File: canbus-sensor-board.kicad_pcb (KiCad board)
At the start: 4 copper layers, 34.5 x 15 mm, 43 parts, among them J1 Conn_ARM_SWD_TagConnect_TC203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, J10 Conn_01x04_Socket, J11 Conn_01x04_Socket, J2 CAN Term, J3 Conn_01x01, J4 Conn_01x01, J5 Conn_01x01, J6 Conn_01x01, J7 Conn_01x01, J8 Conn_01x02_Socket, J9 Conn_01x02_Socket, Q1 AO3400A, Q2 AO3400A, Q3 AO3400A, Q4 AO3400A, U1 L78L05_SOT89, U2 XC6206PxxxMR, U3 STM32F103C8Tx, U4 MCP2551-I-SN

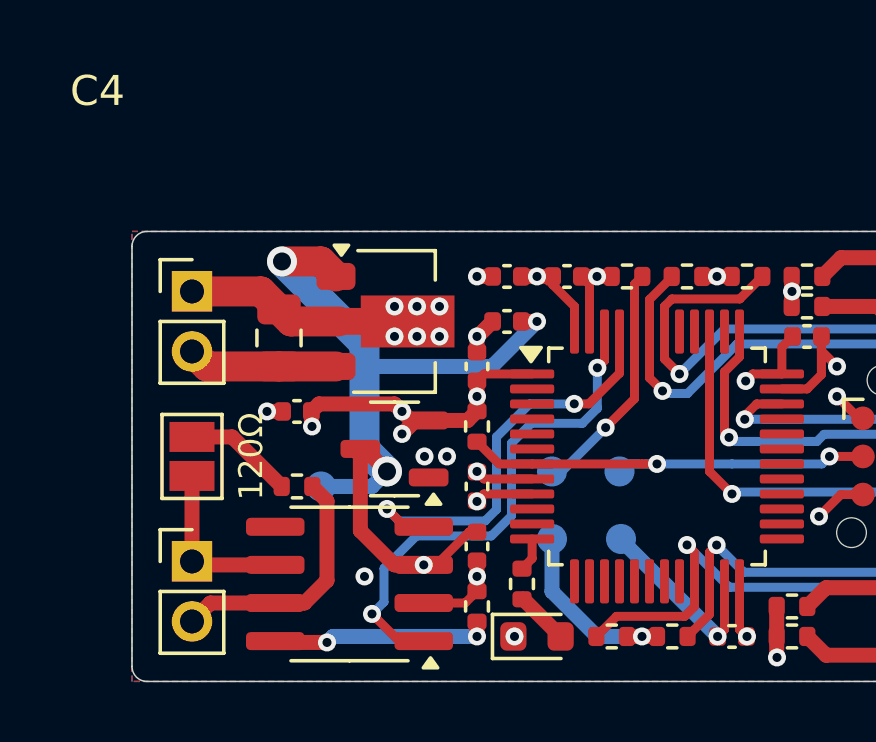
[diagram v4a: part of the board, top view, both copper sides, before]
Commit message: Also make 5V cap larger to have more error margin
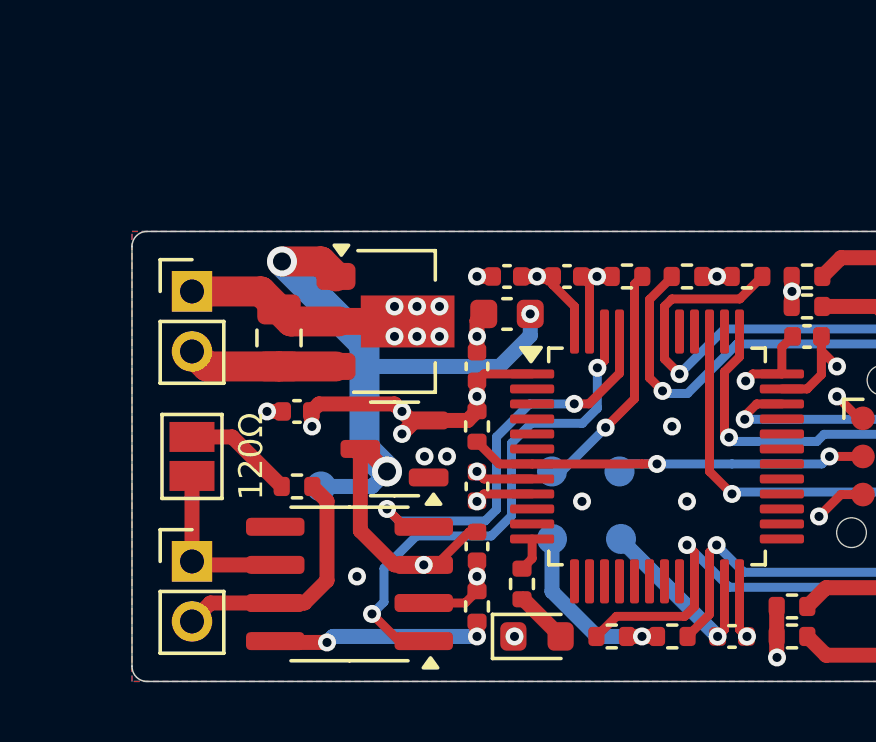
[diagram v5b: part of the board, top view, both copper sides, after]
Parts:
- C2: value 10u -> 10u >5V; footprint Capacitor_SMD:C_0402_1005Metric -> Capacitor_SMD:C_0603_1608Metric
- moved C2 0.25 mm to (35.0, 35.2)
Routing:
- net GND: track 27.8 -> 27.9 mm, vias 21 -> 24
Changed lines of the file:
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@@
 		(tags "SOT-89-3")
 		(property "Reference" "U1"
-			(at 0 -3.5 0)
+			(at -9.9 -7.68 0)
 			(layer "User.1")
 			(hide yes)
@@
 			)
 		)
-		(property "Reference" "C4"
-			(at -9.9 -7.68 0)
-			(layer "F.SilkS")
+		(property "Datasheet" "http://www.st.com/content/ccc/resource/technical/document/datasheet/15/55/e5/aa/23/5b/43/fd/CD00000446.pdf/files/CD00000446.pdf/jcr:content/translations/en.CD00000446.pdf"
+			(at 0 0 0)
+			(unlocked yes)
+			(layer "F.Fab")
+			(hide yes)
 			(effects
 				(font
@@
 			)
 		)
-		(property "Datasheet" "http://www.st.com/content/ccc/resource/technical/document/datasheet/15/55/e5/aa/23/5b/43/fd/CD00000446.pdf/files/CD00000446.pdf/jcr:content/translations/en.CD00000446.pdf"
-			(at 0 0 0)
-			(unlocked yes)
-			(layer "F.Fab")
-			(hide yes)
-			(effects
-				(font
-					(size 1 1)
-					(thickness 0.15)
-				)
-			)
-		)
 		(property ki_fp_filters "SOT?89*")
 		(sheetname "Root")
@@
 		(tags "capacitor")
 		(property "Reference" "C1"
-			(at 0 -1.68 270)
+			(at 0 -1.68 -90)
 			(layer "User.1")
 			(hide yes)
@@
 		)
 		(property "Value" "10u >24V"
-			(at 0 1.68 270)
+			(at 0 1.68 -90)
 			(layer "F.Fab")
 			(effects
@@
 		)
 		(fp_text user "${REFERENCE}"
-			(at 0 0 270)
+			(at 0 0 -90)
 			(layer "F.Fab")
 			(effects
@@
 		)
 	)
-	(footprint "Capacitor_SMD:C_0402_1005Metric"
+	(footprint "Capacitor_SMD:C_0603_1608Metric"
 		(layer "F.Cu")
-		(at 35 35.5 180)
-		(descr "Capacitor SMD 0402 (1005 Metric), square (rectangular) end terminal, IPC_7351 nominal, (Body size source: IPC-SM-782 page 76, https://www.pcb-3d.com/wordpress/wp-content/uploads/ipc-sm-782a_amendment_1_and_2.pdf), generated with kicad-footprint-generator")
+		(at 35 35.25 180)
+		(descr "Capacitor SMD 0603 (1608 Metric), square (rectangular) end terminal, IPC_7351 nominal, (Body size source: IPC-SM-782 page 76, https://www.pcb-3d.com/wordpress/wp-content/uploads/ipc-sm-782a_amendment_1_and_2.pdf), generated with kicad-footprint-generator")
 		(tags "capacitor")
 		(property "Reference" "C2"
-			(at 0 -1.16 180)
+			(at 0 -1.43 180)
 			(layer "User.1")
 			(hide yes)
@@
 			)
 		)
-		(property "Value" "10u"
-			(at 0 1.16 180)
+		(property "Value" "10u >5V"
+			(at 0 1.43 180)
 			(layer "F.Fab")
 			(effects
@@
 			)
 		)
-		(property "Footprint" "Capacitor_SMD:C_0402_1005Metric"
+		(property "Footprint" "Capacitor_SMD:C_0603_1608Metric"
 			(at 0 0 180)
 			(unlocked yes)
@@
 			)
 		)
-		(property "MPN" "C15525"
+		(property "MPN" "C19702"
 			(at 0 0 180)
 			(unlocked yes)
@@
 		(attr smd)
 		(fp_line
-			(start -0.107836 0.36)
-			(end 0.107836 0.36)
+			(start -0.14058 0.51)
+			(end 0.14058 0.51)
 			(stroke
 				(width 0.12)
@@
 		)
 		(fp_line
-			(start -0.107836 -0.36)
-			(end 0.107836 -0.36)
+			(start -0.14058 -0.51)
+			(end 0.14058 -0.51)
 			(stroke
 				(width 0.12)
@@
 		)
 		(fp_line
-			(start 0.91 0.46)
-			(end -0.91 0.46)
+			(start 1.48 0.73)
+			(end -1.48 0.73)
 			(stroke
 				(width 0.05)
@@
 		)
 		(fp_line
-			(start 0.91 -0.46)
-			(end 0.91 0.46)
+			(start 1.48 -0.73)
+			(end 1.48 0.73)
 			(stroke
 				(width 0.05)
@@
 		)
 		(fp_line
-			(start -0.91 0.46)
-			(end -0.91 -0.46)
+			(start -1.48 0.73)
+			(end -1.48 -0.73)
 			(stroke
 				(width 0.05)
@@
 		)
 		(fp_line
-			(start -0.91 -0.46)
-			(end 0.91 -0.46)
+			(start -1.48 -0.73)
+			(end 1.48 -0.73)
 			(stroke
 				(width 0.05)
@@
 		)
 		(fp_line
-			(start 0.5 0.25)
-			(end -0.5 0.25)
+			(start 0.8 0.4)
+			(end -0.8 0.4)
 			(stroke
 				(width 0.1)
@@
 		)
 		(fp_line
-			(start 0.5 -0.25)
-			(end 0.5 0.25)
+			(start 0.8 -0.4)
+			(end 0.8 0.4)
 			(stroke
 				(width 0.1)
@@
 		)
 		(fp_line
-			(start -0.5 0.25)
-			(end -0.5 -0.25)
+			(start -0.8 0.4)
+			(end -0.8 -0.4)
 			(stroke
 				(width 0.1)
@@
 		)
 		(fp_line
-			(start -0.5 -0.25)
-			(end 0.5 -0.25)
+			(start -0.8 -0.4)
+			(end 0.8 -0.4)
 			(stroke
 				(width 0.1)
@@
 			(effects
 				(font
-					(size 0.25 0.25)
-					(thickness 0.04)
+					(size 0.4 0.4)
+					(thickness 0.06)
 				)
 			)
 		)
 		(pad "1" smd roundrect
-			(at -0.48 0 180)
-			(size 0.56 0.62)
+			(at -0.775 0 180)
+			(size 0.9 0.95)
 			(layers "F.Cu" "F.Paste" "F.Mask")
 			(roundrect_rratio 0.25)
@@
 		)
 		(pad "2" smd roundrect
-			(at 0.48 0 180)
-			(size 0.56 0.62)
+			(at 0.775 0 180)
+			(size 0.9 0.95)
 			(layers "F.Cu" "F.Paste" "F.Mask")
 			(roundrect_rratio 0.25)
@@
 			(pintype "passive")
 		)
-		(model "${KICAD8_3DMODEL_DIR}/Capacitor_SMD.3dshapes/C_0402_1005Metric.wrl"
+		(model "${KICAD8_3DMODEL_DIR}/Capacitor_SMD.3dshapes/C_0603_1608Metric.wrl"
 			(offset
 				(xyz 0 0 0)
@@
 	)
 	(segment
-		(start 36 35.5)
-		(end 35.48 35.5)
-		(width 0.5)
-		(layer "F.Cu")
-		(net 5)
-	)
-	(segment
 		(start 43.99 46.69)
 		(end 44 46.7)
@@
 	)
 	(via
-		(at 36 35.5)
+		(at 35.775 35.25)
 		(size 0.6)
 		(drill 0.3)
@@
 	)
 	(segment
+		(start 37.810661 35.25)
+		(end 35.775 35.25)
+		(width 0.5)
+		(layer "In2.Cu")
+		(net 5)
+	)
+	(segment
 		(start 45.625 33.375)
 		(end 49.875 33.375)
@@
 	)
 	(segment
-		(start 36 35.5)
-		(end 37.560661 35.5)
-		(width 0.5)
-		(layer "In2.Cu")
-		(net 5)
-	)
-	(segment
 		(start 51 45.5)
 		(end 49.75 46.75)
@@
 	)
 	(segment
-		(start 37.560661 35.5)
-		(end 39.810661 33.25)
+		(start 33.689339 46.75)
+		(end 32.225 45.285661)
 		(width 0.5)
 		(layer "In2.Cu")
@@
 	)
 	(segment
-		(start 33.689339 46.75)
-		(end 32.225 45.285661)
+		(start 39.810661 33.25)
+		(end 37.810661 35.25)
 		(width 0.5)
 		(layer "In2.Cu")
@@
 	)
 	(segment
-		(start 34.5 37)
+		(start 34.75 37)
 		(end 30.25 37)
 		(width 0.5)
@@
 	)
 	(segment
-		(start 30.25 39.75)
-		(end 31 40.5)
-		(width 1)
+		(start 35.775 35.25)
+		(end 35.775 35.975)
+		(width 0.5)
 		(layer "B.Cu")
 		(net 5)
 	)
 	(segment
-		(start 30.5 41)
-		(end 31 40.5)
+		(start 35.775 35.975)
+		(end 34.75 37)
 		(width 0.5)
 		(layer "B.Cu")
@@
 	)
 	(segment
-		(start 36 35.5)
-		(end 34.5 37)
+		(start 30.25 39.75)
+		(end 31 40.5)
+		(width 1)
+		(layer "B.Cu")
+		(net 5)
+	)
+	(segment
+		(start 30.5 41)
+		(end 31 40.5)
 		(width 0.5)
 		(layer "B.Cu")
@@
 	)
 	(segment
-		(start 34 36.52)
-		(end 34 36)
-		(width 0.5)
-		(layer "F.Cu")
-		(net 6)
-	)
-	(segment
 		(start 45.00312 37.75)
 		(end 45.48 37.27312)
@@
 	)
 	(segment
+		(start 34 36)
+		(end 34 35.475)
+		(width 0.5)
+		(layer "F.Cu")
+		(net 6)
+	)
+	(segment
 		(start 44.1625 37.75)
 		(end 45.00312 37.75)
@@
 	)
 	(segment
-		(start 34 36)
-		(end 34.02 36)
-		(width 0.5)
-		(layer "F.Cu")
-		(net 6)
-	)
-	(segment
 		(start 46.865 41.27)
 		(end 46.13 41.27)
@@
 	)
 	(segment
+		(start 34 35.475)
+		(end 34.225 35.25)
+		(width 0.5)
+		(layer "F.Cu")
+		(net 6)
+	)
+	(segment
 		(start 27.8 35.5)
 		(end 29.3875 35.5)
@@
 	)
 	(segment
+		(start 34 36.52)
+		(end 34 36)
+		(width 0.5)
+		(layer "F.Cu")
+		(net 6)
+	)
+	(segment
 		(start 24.5 34.5)
 		(end 26.8 34.5)
@@
 	)
 	(segment
-		(start 34.02 36)
-		(end 34.52 35.5)
-		(width 0.5)
-		(layer "F.Cu")
-		(net 6)
-	)
-	(segment
 		(start 34.52 34)
 		(end 34 34)
@@
 	)
 	(via
-		(at 45.4 42)
+		(at 34 36)
 		(size 0.6)
 		(drill 0.3)
 		(layers "F.Cu" "B.Cu")
+		(free yes)
 		(net 6)
 	)
 	(via
-		(at 32.75 35)
+		(at 37.5 41.5)
 		(size 0.6)
 		(drill 0.3)
 		(layers "F.Cu" "B.Cu")
+		(free yes)
 		(net 6)
 	)
 	(via
-		(at 38 34)
+		(at 41 41.5)
 		(size 0.6)
 		(drill 0.3)
 		(layers "F.Cu" "B.Cu")
+		(free yes)
 		(net 6)
 	)
 	(via
-		(at 34 34)
+		(at 40.5 39)
 		(size 0.6)
 		(drill 0.3)
 		(layers "F.Cu" "B.Cu")
+		(free yes)
 		(net 6)
 	)
 	(via
-		(at 30.25 44)
+		(at 45.4 42)
 		(size 0.6)
 		(drill 0.3)
 		(layers "F.Cu" "B.Cu")
-		(free yes)
 		(net 6)
 	)
 	(via
-		(at 34 36)
+		(at 32.75 35)
+		(size 0.6)
+		(drill 0.3)
+		(layers "F.Cu" "B.Cu")
+		(net 6)
+	)
+	(via
+		(at 38 34)
+		(size 0.6)
+		(drill 0.3)
+		(layers "F.Cu" "B.Cu")
+		(net 6)
+	)
+	(via
+		(at 34 34)
 		(size 0.6)
 		(drill 0.3)
@@
 		(net 6)
 	)
+	(via
+		(at 30 44)
+		(size 0.6)
+		(drill 0.3)
+		(layers "F.Cu" "B.Cu")
+		(free yes)
+		(net 6)
+	)
